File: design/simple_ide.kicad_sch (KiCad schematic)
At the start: 14 parts, among them IC1 ATF22V10C-15PU, IC2 ATF22V10C-15PU, IC3 74ACT245, IC4 74ACT245, J2 Conn_02x22_Odd_Even

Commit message: Recheck WinCUPL against design
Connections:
- net A10: now also IC1.17 (I/O_4); no longer IC1.19 (I/O_6)
- net A11: now also IC1.16 (I/O_3); no longer IC1.18 (I/O_5)
- net A12: now also IC1.15 (I/O_2); no longer IC1.17 (I/O_4)
- net A13: now also IC1.14 (I/O_1); no longer IC1.5 (IN_3)
- net A14: now also IC1.13 (IN_10); no longer IC1.6 (IN_4)
- net A15: now also IC1.6 (IN_4); no longer IC1.7 (IN_5)
- net A16: now also IC1.7 (IN_5); no longer IC1.8 (IN_6)
- net A17: now also IC1.8 (IN_6); no longer IC1.9 (IN_7)
- net A18: now also IC1.9 (IN_7); no longer IC1.10 (IN_8)
- net A19: now also IC1.10 (IN_8); no longer IC1.11 (IN_9)
- net A5: now also IC1.22 (I/O_9); no longer IC2.4 (IN/PD)
- net A6: now also IC1.21 (I/O_8); no longer IC1.23 (I/O_10)
- net A7: now also IC1.20 (I/O_7); no longer IC1.22 (I/O_9)
- net A8: now also IC1.19 (I/O_6); no longer IC1.21 (I/O_8)
- net A9: now also IC1.18 (I/O_5); no longer IC1.20 (I/O_7)
- net AS: now also IC1.11 (IN_9)
- net IDERDY: now also IC2.3 (IN_2)
- net ~{IDECS}: now also IC1.23 (I/O_10), IC2.22 (I/O_9); no longer IC1.13 (IN_10), IC2.3 (IN_2)
- no-connect marks 20 -> 23

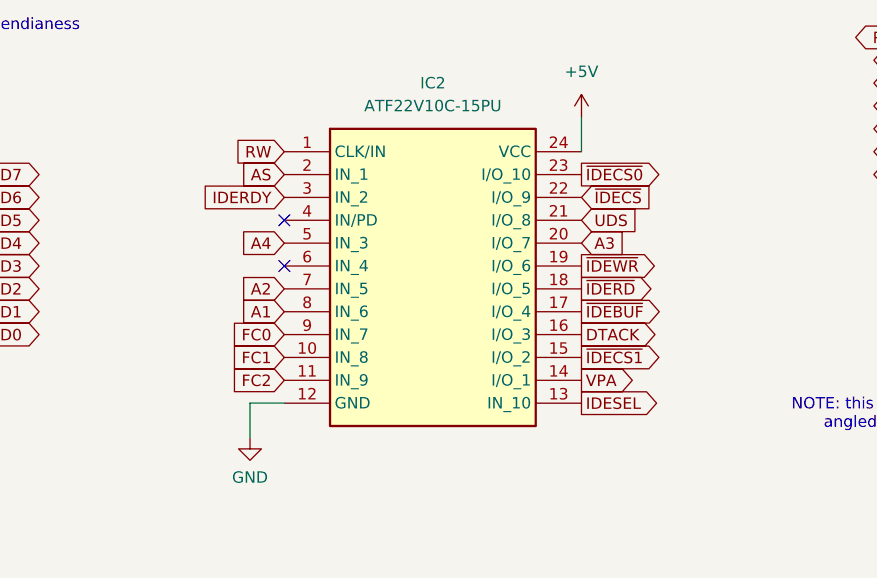
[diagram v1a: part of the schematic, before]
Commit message: Compile Wincuple and reroute pins to ensure outputs on output pins
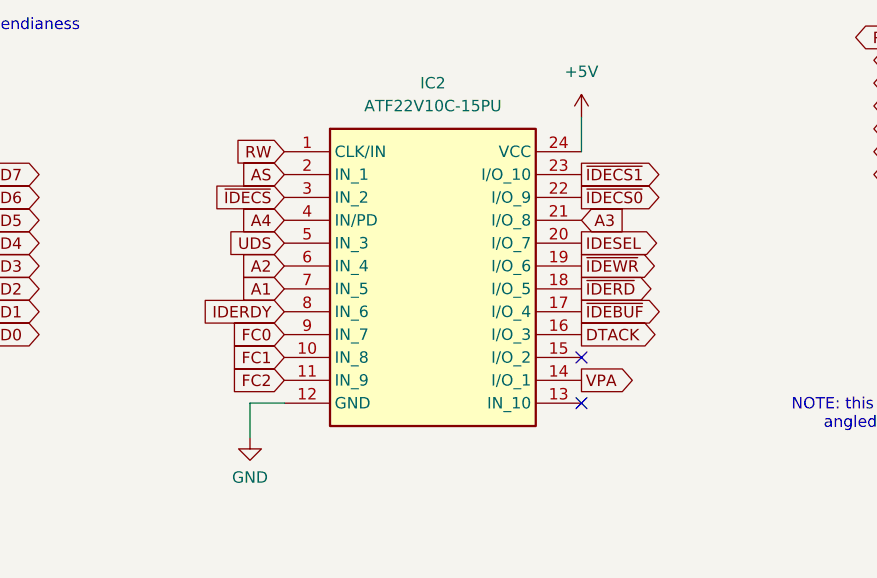
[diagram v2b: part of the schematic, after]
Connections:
- net A1: now also IC2.7 (IN_5); no longer IC2.8 (IN_6)
- net A2: now also IC2.6 (IN_4); no longer IC2.7 (IN_5)
- net A3: now also IC2.21 (I/O_8); no longer IC2.20 (I/O_7)
- net A4: now also IC2.4 (IN/PD); no longer IC2.5 (IN_3)
- net IDERDY: now also IC2.8 (IN_6); no longer IC2.3 (IN_2)
- net IDESEL: now also IC2.20 (I/O_7); no longer IC2.13 (IN_10)
- net UDS: now also IC2.5 (IN_3); no longer IC2.21 (I/O_8)
- net ~{IDECS0}: now also IC2.22 (I/O_9); no longer IC2.23 (I/O_10)
- net ~{IDECS1}: now also IC2.23 (I/O_10); no longer IC2.15 (I/O_2)
- net ~{IDECS}: now also IC2.3 (IN_2); no longer IC2.22 (I/O_9)

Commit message: Start work on v2
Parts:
- removed D2: LED, LED_THT:LED_D5.0mm, symbol Device:LED
- removed R1: 1K, Resistor_THT:R_Axial_DIN0207_L6.3mm_D2.5mm_P7.62mm_Horizontal, symbol Device:R
- removed R2, R3: 4K7, Resistor_THT:R_Axial_DIN0207_L6.3mm_D2.5mm_P7.62mm_Horizontal, symbol Device:R
- IC3, IC4: value 74ACT245 -> 74245
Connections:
- net IDEBUF is gone; now on net ~{IDEBUF}: IC3.19 (CE), IC4.19 (CE)
- net ~{RESET} is gone; now on net RESET: J2.1 (Pin_1)
- net A1: now also IC2.14 (I/O_1); no longer IC2.7 (IN_5)
- net A2: now also IC2.13 (IN_10); no longer IC2.6 (IN_4)
- net FC0: no longer IC2.9 (IN_7)
- net FC1: no longer IC2.10 (IN_8)
- net FC2: no longer IC2.11 (IN_9)
- net VPA: no longer IC2.14 (I/O_1)
- net IDERDY: no longer names the net of IC2.8 (IN_6)
- net IDERDY: no longer J2.27 (Pin_27)
- net INTRQ: no longer names the net of J2.31 (Pin_31)
- net ~{DASP}: no longer names the net of J2.39 (Pin_39)
- no-connect marks 23 -> 37
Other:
- note removed: "wire CPU_SPACE = (FC0 && FC1 && FC2); assign IDECS_n = !(!CPU_SPACE && !IOSEL_n && (A[19:6] == 13'b10000000000001)); assign IDECS0_n = !(!IDECS_n && !A5 && A4); assign IDECS1_n = !(!IDECS_n && A5 && !A4); assign IDERD_n = !(RW && !AS_n && !UDS_n); assign IDEWR_n = !(!RW && !AS_n && !UDS_n); assign IDEBUF_n = ~(~IDECS0_n || ~IDECS1_n); wire IDE_SELECTED = ~AS_n && (~IDECS0_n || ~IDECS1_n); assign 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"
- moved on the sheet: J2

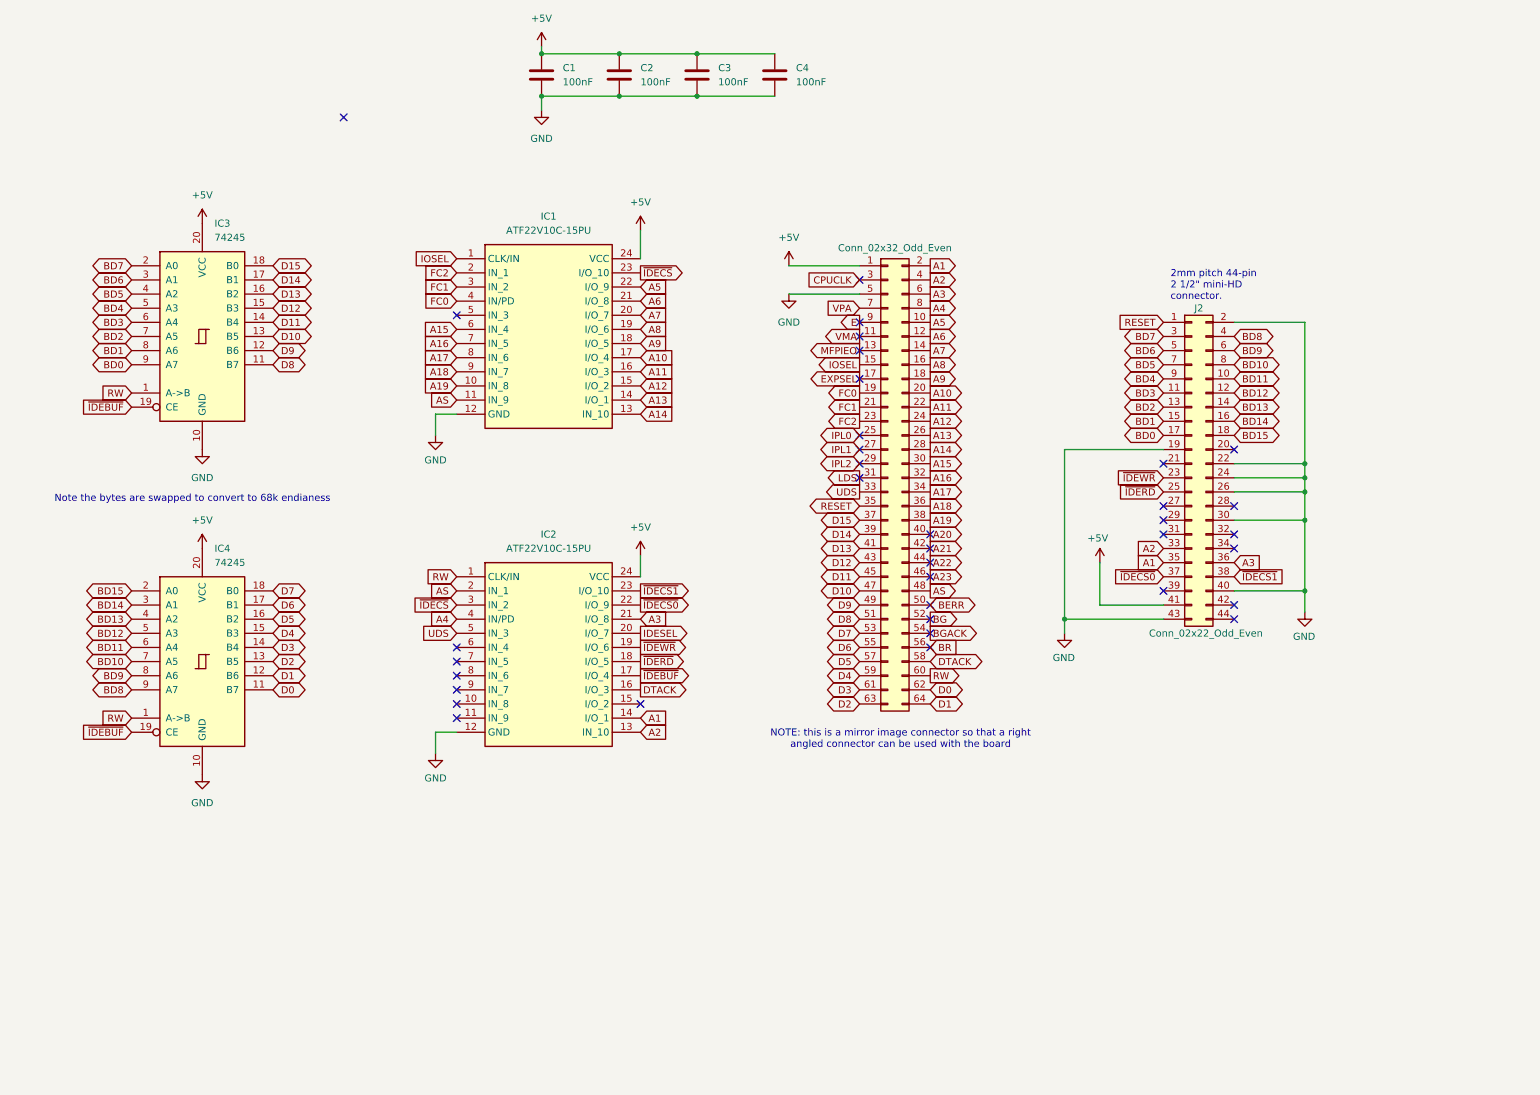
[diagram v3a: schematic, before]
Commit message: First test of v2 production files .. seems to read a disk ok
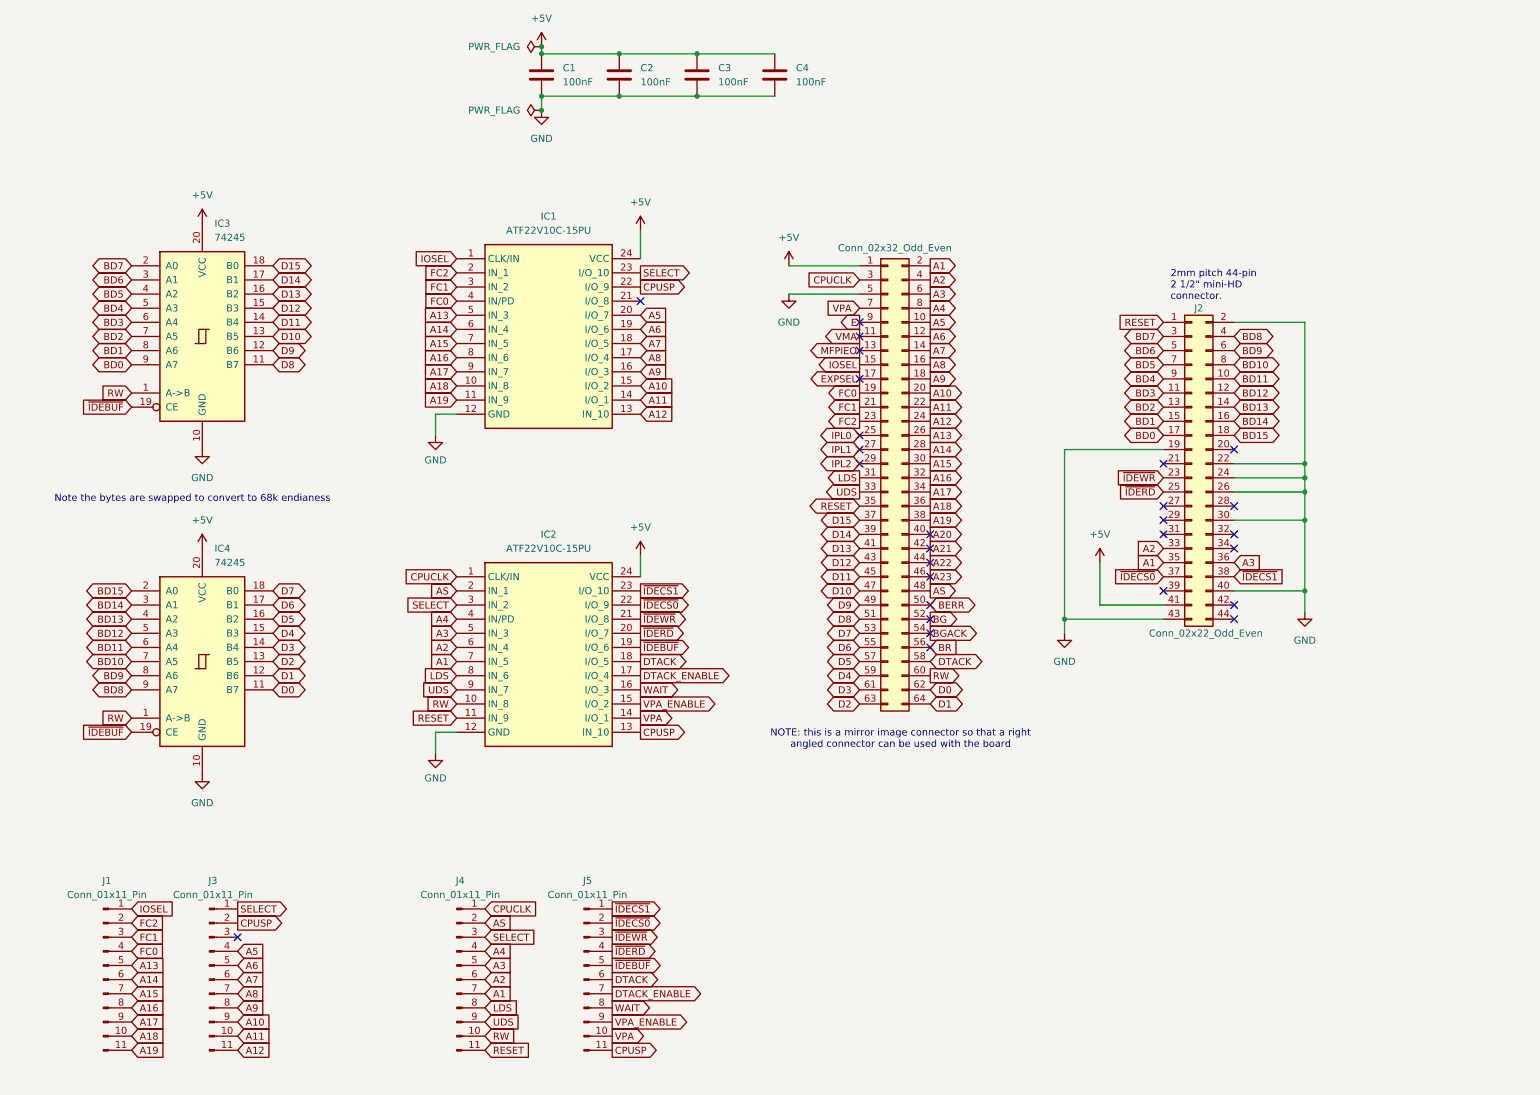
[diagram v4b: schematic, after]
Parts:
- added J1, J3, J4, J5: Conn_01x11_Pin, Connector_PinHeader_2.54mm:PinHeader_1x11_P2.54mm_Vertical, symbol Connector:Conn_01x11_Pin
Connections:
- net IDESEL is gone; now on net ~{IDERD}: IC2.20 (I/O_7)
- net A1: now also IC2.7 (IN_5), J4.7 (Pin_7); no longer IC2.14 (I/O_1)
- net A10: now also IC1.15 (I/O_2), J3.9 (Pin_9); no longer IC1.17 (I/O_4)
- net A11: now also IC1.14 (I/O_1), J3.10 (Pin_10); no longer IC1.16 (I/O_3)
- net A12: now also IC1.13 (IN_10), J3.11 (Pin_11); no longer IC1.15 (I/O_2)
- net A13: now also IC1.5 (IN_3), J1.5 (Pin_5); no longer IC1.14 (I/O_1)
- net A14: now also IC1.6 (IN_4), J1.6 (Pin_6); no longer IC1.13 (IN_10)
- net A15: now also IC1.7 (IN_5), J1.7 (Pin_7); no longer IC1.6 (IN_4)
- net A16: now also IC1.8 (IN_6), J1.8 (Pin_8); no longer IC1.7 (IN_5)
- net A17: now also IC1.9 (IN_7), J1.9 (Pin_9); no longer IC1.8 (IN_6)
- net A18: now also IC1.10 (IN_8), J1.10 (Pin_10); no longer IC1.9 (IN_7)
- net A19: now also IC1.11 (IN_9), J1.11 (Pin_11); no longer IC1.10 (IN_8)
- net A2: now also IC2.6 (IN_4), J4.6 (Pin_6); no longer IC2.13 (IN_10)
- net A3: now also IC2.5 (IN_3), J4.5 (Pin_5); no longer IC2.21 (I/O_8)
- net A4: now also J4.4 (Pin_4)
- net A5: now also IC1.20 (I/O_7), J3.4 (Pin_4); no longer IC1.22 (I/O_9)
- net A6: now also IC1.19 (I/O_6), J3.5 (Pin_5); no longer IC1.21 (I/O_8)
- net A7: now also IC1.18 (I/O_5), J3.6 (Pin_6); no longer IC1.20 (I/O_7)
- net A8: now also IC1.17 (I/O_4), J3.7 (Pin_7); no longer IC1.19 (I/O_6)
- net A9: now also IC1.16 (I/O_3), J3.8 (Pin_8); no longer IC1.18 (I/O_5)
- net AS: now also J4.2 (Pin_2); no longer IC1.11 (IN_9)
- net CPUCLK: now also IC2.1 (CLK/IN), J4.1 (Pin_1)
- net DTACK: now also IC2.18 (I/O_5), J5.6 (Pin_6); no longer IC2.16 (I/O_3)
- net FC0: now also J1.4 (Pin_4)
- net FC1: now also J1.3 (Pin_3)
- net FC2: now also J1.2 (Pin_2)
- net IOSEL: now also J1.1 (Pin_1)
- net LDS: now also IC2.8 (IN_6), J4.8 (Pin_8)
- net RESET: now also IC2.11 (IN_9), J4.11 (Pin_11)
- net RW: now also IC2.10 (IN_8), J4.10 (Pin_10); no longer IC2.1 (CLK/IN)
- net UDS: now also IC2.9 (IN_7), J4.9 (Pin_9); no longer IC2.5 (IN_3)
- net VPA: now also IC2.14 (I/O_1), J5.10 (Pin_10)
- net ~{IDEBUF}: now also IC2.19 (I/O_6), J5.5 (Pin_5); no longer IC2.17 (I/O_4)
- net ~{IDECS0}: now also J5.2 (Pin_2)
- net ~{IDECS1}: now also J5.1 (Pin_1)
- net ~{IDERD}: now also J5.4 (Pin_4); no longer IC2.18 (I/O_5)
- net ~{IDEWR}: now also IC2.21 (I/O_8), J5.3 (Pin_3); no longer IC2.19 (I/O_6)
- net VPA_ENABLE: now reaches IC2.15 (I/O_2)
- net VPA_ENABLE: now also J5.9 (Pin_9)
- net ~{IDECS} renamed SELECT
- net SELECT: now also J3.1 (Pin_1), J4.3 (Pin_3)
- new net CPUSP: IC1.22 (I/O_9), IC2.13 (IN_10), J3.2 (Pin_2), J5.11 (Pin_11)
- new net DTACK_ENABLE: IC2.17 (I/O_4), J5.7 (Pin_7)
- new net WAIT: IC2.16 (I/O_3), J5.8 (Pin_8)
- no-connect marks 37 -> 28
